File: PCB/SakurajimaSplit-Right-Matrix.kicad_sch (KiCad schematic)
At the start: 42 parts

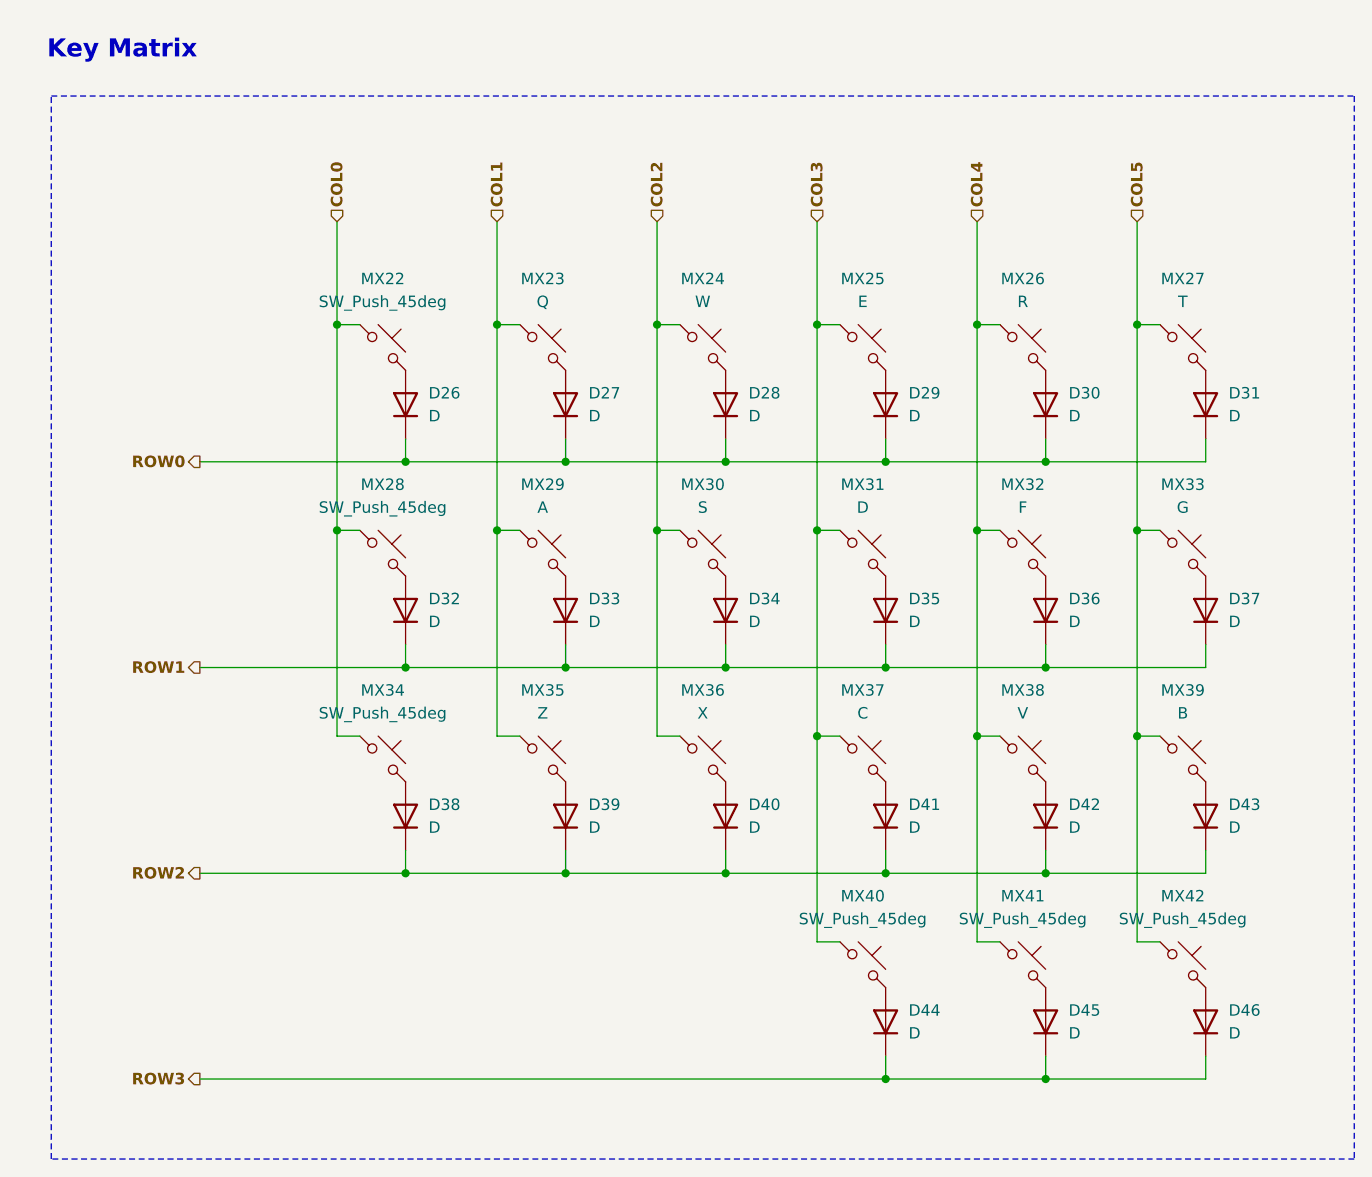
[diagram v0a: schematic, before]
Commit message: feat(sch): design right half of the keyboard
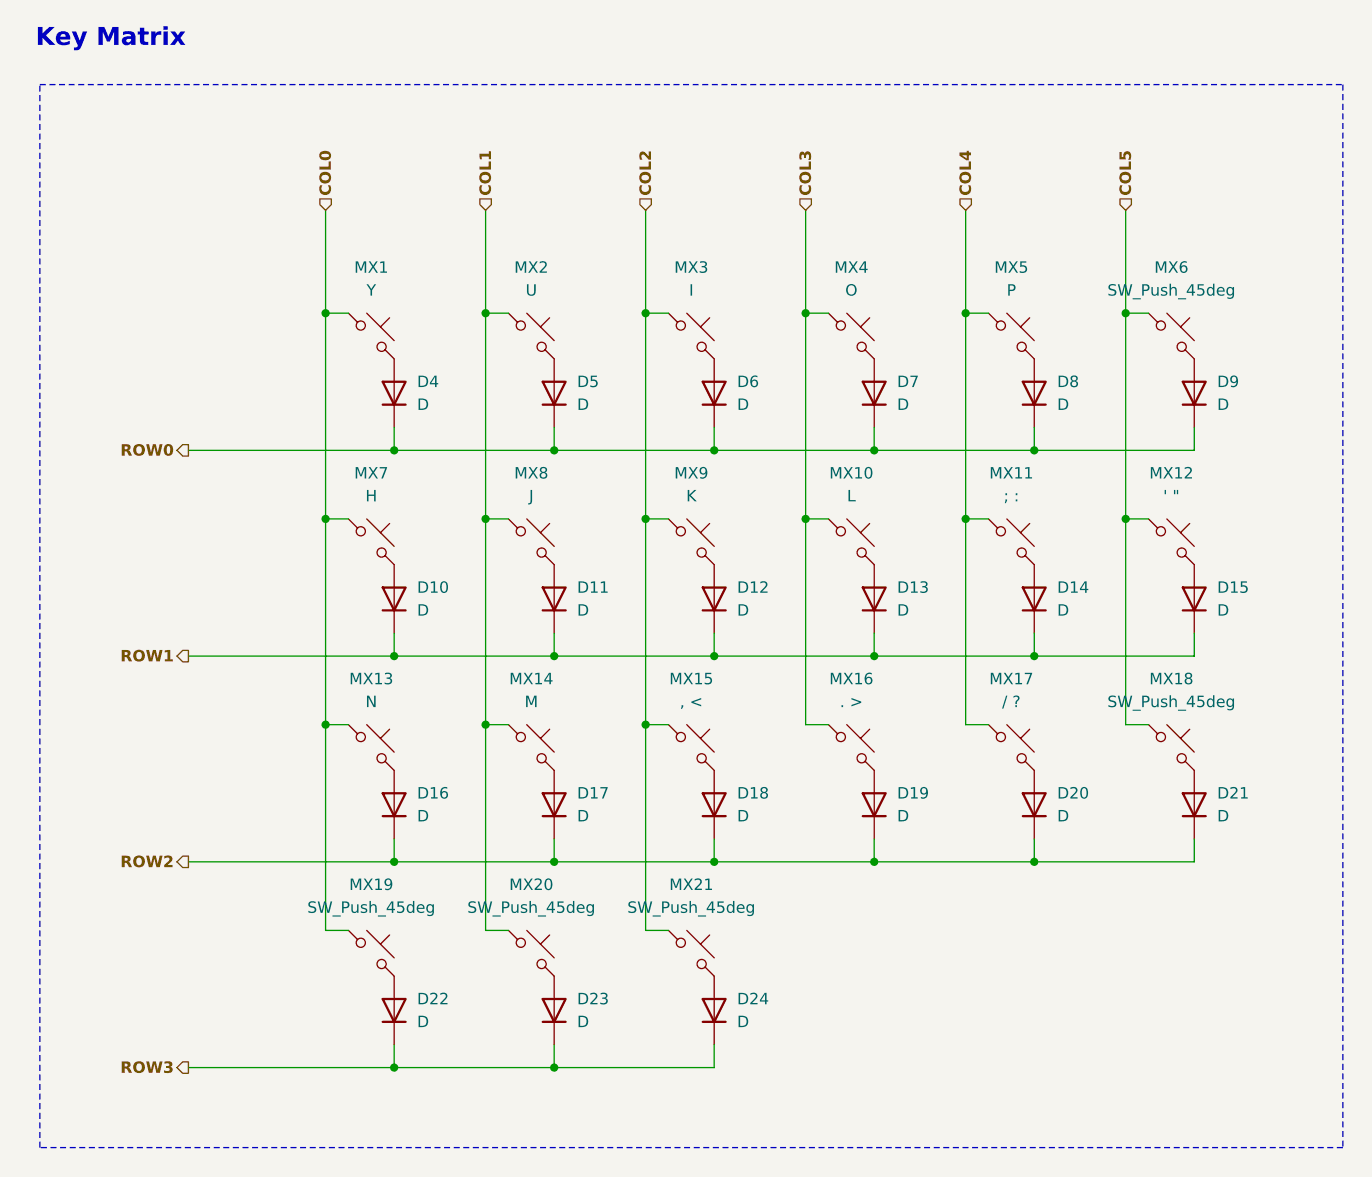
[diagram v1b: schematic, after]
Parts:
- removed D26, D27, D28, D29, D30, D31, D32, D33, D34, D35, D36, D37, D38, D39, D40, D41, D42, D43, D44, D45, D46: D, symbol Device:D
- removed MX22, MX28, MX34, MX40, MX41, MX42: SW_Push_45deg, symbol Switch:SW_Push_45deg
- removed MX23: Q, symbol Switch:SW_Push_45deg
- removed MX24: W, symbol Switch:SW_Push_45deg
- removed MX25: E, symbol Switch:SW_Push_45deg
- removed MX26: R, symbol Switch:SW_Push_45deg
- removed MX27: T, symbol Switch:SW_Push_45deg
- removed MX29: A, symbol Switch:SW_Push_45deg
- removed MX30: S, symbol Switch:SW_Push_45deg
- removed MX31: D, symbol Switch:SW_Push_45deg
- removed MX32: F, symbol Switch:SW_Push_45deg
- removed MX33: G, symbol Switch:SW_Push_45deg
- removed MX35: Z, symbol Switch:SW_Push_45deg
- removed MX36: X, symbol Switch:SW_Push_45deg
- removed MX37: C, symbol Switch:SW_Push_45deg
- removed MX38: V, symbol Switch:SW_Push_45deg
- removed MX39: B, symbol Switch:SW_Push_45deg
- added D10, D11, D12, D13, D14, D15, D16, D17, D18, D19, D20, D21, D22, D23, D24, D4, D5, D6, D7, D8, D9: D, symbol Device:D
- added MX1: Y, symbol Switch:SW_Push_45deg
- added MX10: L, symbol Switch:SW_Push_45deg
- added MX11: ; :, symbol Switch:SW_Push_45deg
- added MX12: ' ", symbol Switch:SW_Push_45deg
- added MX13: N, symbol Switch:SW_Push_45deg
- added MX14: M, symbol Switch:SW_Push_45deg
- added MX15: , <, symbol Switch:SW_Push_45deg
- added MX16: . >, symbol Switch:SW_Push_45deg
- added MX17: / ?, symbol Switch:SW_Push_45deg
- added MX18, MX19, MX20, MX21, MX6: SW_Push_45deg, symbol Switch:SW_Push_45deg
- added MX2: U, symbol Switch:SW_Push_45deg
- added MX3: I, symbol Switch:SW_Push_45deg
- added MX4: O, symbol Switch:SW_Push_45deg
- added MX5: P, symbol Switch:SW_Push_45deg
- added MX7: H, symbol Switch:SW_Push_45deg
- added MX8: J, symbol Switch:SW_Push_45deg
- added MX9: K, symbol Switch:SW_Push_45deg
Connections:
- net COL0: now also MX1.1, MX13.1, MX19.1, MX7.1
- net COL1: now also MX14.1, MX2.1, MX20.1, MX8.1
- net COL2: now also MX15.1, MX21.1, MX3.1, MX9.1
- net COL3: now also MX10.1, MX16.1, MX4.1
- net COL4: now also MX11.1, MX17.1, MX5.1
- net COL5: now also MX12.1, MX18.1, MX6.1
- net ROW0: now also D4.1 (K), D5.1 (K), D6.1 (K), D7.1 (K), D8.1 (K), D9.1 (K)
- net ROW1: now also D10.1 (K), D11.1 (K), D12.1 (K), D13.1 (K), D14.1 (K), D15.1 (K)
- net ROW2: now also D16.1 (K), D17.1 (K), D18.1 (K), D19.1 (K), D20.1 (K), D21.1 (K)
- net ROW3: now also D22.1 (K), D23.1 (K), D24.1 (K)
- new net: D4.2 (A), MX1.2
- new net: D11.2 (A), MX8.2
- new net: D17.2 (A), MX14.2
- new net: D8.2 (A), MX5.2
- new net: D19.2 (A), MX16.2
- new net: D21.2 (A), MX18.2
- new net: D10.2 (A), MX7.2
- new net: D6.2 (A), MX3.2
- new net: D7.2 (A), MX4.2
- new net: D24.2 (A), MX21.2
- new net: D23.2 (A), MX20.2
- new net: D15.2 (A), MX12.2
- new net: D14.2 (A), MX11.2
- new net: D22.2 (A), MX19.2
- new net: D5.2 (A), MX2.2
- new net: D12.2 (A), MX9.2
- new net: D13.2 (A), MX10.2
- new net: D9.2 (A), MX6.2
- new net: D16.2 (A), MX13.2
- new net: D20.2 (A), MX17.2
- new net: D18.2 (A), MX15.2

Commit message: feat(pcb): assign all footprints
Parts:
- D28: renamed from D4; footprint (none) -> Diode_SMD:D_SOD-123
- D29: renamed from D5; footprint (none) -> Diode_SMD:D_SOD-123
- D30: renamed from D6; footprint (none) -> Diode_SMD:D_SOD-123
- D31: renamed from D7; footprint (none) -> Diode_SMD:D_SOD-123
- D32: renamed from D8; footprint (none) -> Diode_SMD:D_SOD-123
- D33: renamed from D9; footprint (none) -> Diode_SMD:D_SOD-123
- D34: renamed from D10; footprint (none) -> Diode_SMD:D_SOD-123
- D35: renamed from D11; footprint (none) -> Diode_SMD:D_SOD-123
- D36: renamed from D12; footprint (none) -> Diode_SMD:D_SOD-123
- D37: renamed from D13; footprint (none) -> Diode_SMD:D_SOD-123
- D38: renamed from D14; footprint (none) -> Diode_SMD:D_SOD-123
- D39: renamed from D15; footprint (none) -> Diode_SMD:D_SOD-123
- D40: renamed from D16; footprint (none) -> Diode_SMD:D_SOD-123
- D41: renamed from D17; footprint (none) -> Diode_SMD:D_SOD-123
- D42: renamed from D18; footprint (none) -> Diode_SMD:D_SOD-123
- D43: renamed from D19; footprint (none) -> Diode_SMD:D_SOD-123
- D44: renamed from D20; footprint (none) -> Diode_SMD:D_SOD-123
- D45: renamed from D21; footprint (none) -> Diode_SMD:D_SOD-123
- D46: renamed from D22; footprint (none) -> Diode_SMD:D_SOD-123
- D47: renamed from D23; footprint (none) -> Diode_SMD:D_SOD-123
- D48: renamed from D24; footprint (none) -> Diode_SMD:D_SOD-123
- MX22: renamed from MX1; footprint (none) -> PCM_marbastlib-mx:SW_MX_1u
- MX23: renamed from MX2; footprint (none) -> PCM_marbastlib-mx:SW_MX_1u
- MX24: renamed from MX3; footprint (none) -> PCM_marbastlib-mx:SW_MX_1u
- MX25: renamed from MX4; footprint (none) -> PCM_marbastlib-mx:SW_MX_1u
- MX26: renamed from MX5; footprint (none) -> PCM_marbastlib-mx:SW_MX_1u
- MX27: renamed from MX6; footprint (none) -> PCM_marbastlib-mx:SW_MX_1u
- MX28: renamed from MX7; footprint (none) -> PCM_marbastlib-mx:SW_MX_1u
- MX29: renamed from MX8; footprint (none) -> PCM_marbastlib-mx:SW_MX_1u
- MX30: renamed from MX9; footprint (none) -> PCM_marbastlib-mx:SW_MX_1u
- MX31: renamed from MX10; footprint (none) -> PCM_marbastlib-mx:SW_MX_1u
- MX32: renamed from MX11; footprint (none) -> PCM_marbastlib-mx:SW_MX_1u
- MX33: renamed from MX12; footprint (none) -> PCM_marbastlib-mx:SW_MX_1u
- MX34: renamed from MX13; footprint (none) -> PCM_marbastlib-mx:SW_MX_1u
- MX35: renamed from MX14; footprint (none) -> PCM_marbastlib-mx:SW_MX_1u
- MX36: renamed from MX15; footprint (none) -> PCM_marbastlib-mx:SW_MX_1u
- MX37: renamed from MX16; footprint (none) -> PCM_marbastlib-mx:SW_MX_1u
- MX38: renamed from MX17; footprint (none) -> PCM_marbastlib-mx:SW_MX_1u
- MX39: renamed from MX18; footprint (none) -> PCM_marbastlib-mx:SW_MX_1u
- MX40: renamed from MX19; footprint (none) -> PCM_marbastlib-mx:SW_MX_1u
- MX41: renamed from MX20; footprint (none) -> PCM_marbastlib-mx:SW_MX_1u
- MX42: renamed from MX21; footprint (none) -> PCM_marbastlib-mx:SW_MX_1u

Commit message: fix(sch): fix matrix diode designators not starting from 1
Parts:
- renumbered D28 to D22, D29 to D23, D30 to D24, D31 to D25, D32 to D26, D33 to D27, D34 to D28, D35 to D29, D36 to D30, D37 to D31, D38 to D32, D39 to D33, D40 to D34, D41 to D35, D42 to D36, D43 to D37, D44 to D38, D45 to D39, D46 to D40, D47 to D41, D48 to D42
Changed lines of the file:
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@@
 		(dnp no)
 		(fields_autoplaced yes)
-		(property "Reference" "D28"
+		(property "Reference" "D22"
 			(at 177.8 111.7599 90)
 			(effects
@@
 			(project "SakurajimaSplit"
 				(path "/2049b6de-7453-46e1-ab60-70116abff9d6/2fb40ee0-3e4b-4e2d-8d4c-b78786a3c10e/177a5d22-8137-4d36-99f5-f50b13e7348e"
-					(reference "D28")
+					(reference "D22")
 					(unit 1)
 				)
@@
 		(dnp no)
 		(fields_autoplaced yes)
-		(property "Reference" "D35"
+		(property "Reference" "D29"
 			(at 195.58 134.6199 90)
 			(effects
@@
 			(project "SakurajimaSplit"
 				(path "/2049b6de-7453-46e1-ab60-70116abff9d6/2fb40ee0-3e4b-4e2d-8d4c-b78786a3c10e/177a5d22-8137-4d36-99f5-f50b13e7348e"
-					(reference "D35")
+					(reference "D29")
 					(unit 1)
 				)
@@
 		(dnp no)
 		(fields_autoplaced yes)
-		(property "Reference" "D41"
+		(property "Reference" "D35"
 			(at 195.58 157.4799 90)
 			(effects
@@
 			(project "SakurajimaSplit"
 				(path "/2049b6de-7453-46e1-ab60-70116abff9d6/2fb40ee0-3e4b-4e2d-8d4c-b78786a3c10e/177a5d22-8137-4d36-99f5-f50b13e7348e"
-					(reference "D41")
+					(reference "D35")
 					(unit 1)
 				)
@@
 		(dnp no)
 		(fields_autoplaced yes)
-		(property "Reference" "D32"
+		(property "Reference" "D26"
 			(at 248.92 111.7599 90)
 			(effects
@@
 			(project "SakurajimaSplit"
 				(path "/2049b6de-7453-46e1-ab60-70116abff9d6/2fb40ee0-3e4b-4e2d-8d4c-b78786a3c10e/177a5d22-8137-4d36-99f5-f50b13e7348e"
-					(reference "D32")
+					(reference "D26")
 					(unit 1)
 				)
@@
 		(dnp no)
 		(fields_autoplaced yes)
-		(property "Reference" "D45"
+		(property "Reference" "D39"
 			(at 266.7 157.4799 90)
 			(effects
@@
 			(project "SakurajimaSplit"
 				(path "/2049b6de-7453-46e1-ab60-70116abff9d6/2fb40ee0-3e4b-4e2d-8d4c-b78786a3c10e/177a5d22-8137-4d36-99f5-f50b13e7348e"
-					(reference "D45")
+					(reference "D39")
 					(unit 1)
 				)
@@
 		(dnp no)
 		(fields_autoplaced yes)
-		(property "Reference" "D30"
+		(property "Reference" "D24"
 			(at 213.36 111.7599 90)
 			(effects
@@
 			(project "SakurajimaSplit"
 				(path "/2049b6de-7453-46e1-ab60-70116abff9d6/2fb40ee0-3e4b-4e2d-8d4c-b78786a3c10e/177a5d22-8137-4d36-99f5-f50b13e7348e"
-					(reference "D30")
+					(reference "D24")
 					(unit 1)
 				)
@@
 		(dnp no)
 		(fields_autoplaced yes)
-		(property "Reference" "D39"
+		(property "Reference" "D33"
 			(at 266.7 134.6199 90)
 			(effects
@@
 			(project "SakurajimaSplit"
 				(path "/2049b6de-7453-46e1-ab60-70116abff9d6/2fb40ee0-3e4b-4e2d-8d4c-b78786a3c10e/177a5d22-8137-4d36-99f5-f50b13e7348e"
-					(reference "D39")
+					(reference "D33")
 					(unit 1)
 				)
@@
 		(dnp no)
 		(fields_autoplaced yes)
-		(property "Reference" "D46"
+		(property "Reference" "D40"
 			(at 177.8 180.3399 90)
 			(effects
@@
 			(project "SakurajimaSplit"
 				(path "/2049b6de-7453-46e1-ab60-70116abff9d6/2fb40ee0-3e4b-4e2d-8d4c-b78786a3c10e/177a5d22-8137-4d36-99f5-f50b13e7348e"
-					(reference "D46")
+					(reference "D40")
 					(unit 1)
 				)
@@
 		(dnp no)
 		(fields_autoplaced yes)
-		(property "Reference" "D29"
+		(property "Reference" "D23"
 			(at 195.58 111.7599 90)
 			(effects
@@
 			(project "SakurajimaSplit"
 				(path "/2049b6de-7453-46e1-ab60-70116abff9d6/2fb40ee0-3e4b-4e2d-8d4c-b78786a3c10e/177a5d22-8137-4d36-99f5-f50b13e7348e"
-					(reference "D29")
+					(reference "D23")
 					(unit 1)
 				)
@@
 		(dnp no)
 		(fields_autoplaced yes)
-		(property "Reference" "D38"
+		(property "Reference" "D32"
 			(at 248.92 134.6199 90)
 			(effects
@@
 			(project "SakurajimaSplit"
 				(path "/2049b6de-7453-46e1-ab60-70116abff9d6/2fb40ee0-3e4b-4e2d-8d4c-b78786a3c10e/177a5d22-8137-4d36-99f5-f50b13e7348e"
-					(reference "D38")
+					(reference "D32")
 					(unit 1)
 				)
@@
 		(dnp no)
 		(fields_autoplaced yes)
-		(property "Reference" "D48"
+		(property "Reference" "D42"
 			(at 213.36 180.3399 90)
 			(effects
@@
 			(project "SakurajimaSplit"
 				(path "/2049b6de-7453-46e1-ab60-70116abff9d6/2fb40ee0-3e4b-4e2d-8d4c-b78786a3c10e/177a5d22-8137-4d36-99f5-f50b13e7348e"
-					(reference "D48")
+					(reference "D42")
 					(unit 1)
 				)
@@
 		(dnp no)
 		(fields_autoplaced yes)
-		(property "Reference" "D34"
+		(property "Reference" "D28"
 			(at 177.8 134.6199 90)
 			(effects
@@
 			(project "SakurajimaSplit"
 				(path "/2049b6de-7453-46e1-ab60-70116abff9d6/2fb40ee0-3e4b-4e2d-8d4c-b78786a3c10e/177a5d22-8137-4d36-99f5-f50b13e7348e"
-					(reference "D34")
+					(reference "D28")
 					(unit 1)
 				)
@@
 		(dnp no)
 		(fields_autoplaced yes)
-		(property "Reference" "D43"
+		(property "Reference" "D37"
 			(at 231.14 157.4799 90)
 			(effects
@@
 			(project "SakurajimaSplit"
 				(path "/2049b6de-7453-46e1-ab60-70116abff9d6/2fb40ee0-3e4b-4e2d-8d4c-b78786a3c10e/177a5d22-8137-4d36-99f5-f50b13e7348e"
-					(reference "D43")
+					(reference "D37")
 					(unit 1)
 				)
@@
 		(dnp no)
 		(fields_autoplaced yes)
-		(property "Reference" "D37"
+		(property "Reference" "D31"
 			(at 231.14 134.6199 90)
 			(effects
@@
 			(project "SakurajimaSplit"
 				(path "/2049b6de-7453-46e1-ab60-70116abff9d6/2fb40ee0-3e4b-4e2d-8d4c-b78786a3c10e/177a5d22-8137-4d36-99f5-f50b13e7348e"
-					(reference "D37")
+					(reference "D31")
 					(unit 1)
 				)
@@
 		(dnp no)
 		(fields_autoplaced yes)
-		(property "Reference" "D33"
+		(property "Reference" "D27"
 			(at 266.7 111.7599 90)
 			(effects
@@
 			(project "SakurajimaSplit"
 				(path "/2049b6de-7453-46e1-ab60-70116abff9d6/2fb40ee0-3e4b-4e2d-8d4c-b78786a3c10e/177a5d22-8137-4d36-99f5-f50b13e7348e"
-					(reference "D33")
+					(reference "D27")
 					(unit 1)
 				)
@@
 		(dnp no)
 		(fields_autoplaced yes)
-		(property "Reference" "D31"
+		(property "Reference" "D25"
 			(at 231.14 111.7599 90)
 			(effects
@@
 			(project "SakurajimaSplit"
 				(path "/2049b6de-7453-46e1-ab60-70116abff9d6/2fb40ee0-3e4b-4e2d-8d4c-b78786a3c10e/177a5d22-8137-4d36-99f5-f50b13e7348e"
-					(reference "D31")
+					(reference "D25")
 					(unit 1)
 				)
@@
 		(dnp no)
 		(fields_autoplaced yes)
-		(property "Reference" "D40"
+		(property "Reference" "D34"
 			(at 177.8 157.4799 90)
 			(effects
@@
 			(project "SakurajimaSplit"
 				(path "/2049b6de-7453-46e1-ab60-70116abff9d6/2fb40ee0-3e4b-4e2d-8d4c-b78786a3c10e/177a5d22-8137-4d36-99f5-f50b13e7348e"
-					(reference "D40")
+					(reference "D34")
 					(unit 1)
 				)
@@
 		(dnp no)
 		(fields_autoplaced yes)
-		(property "Reference" "D36"
+		(property "Reference" "D30"
 			(at 213.36 134.6199 90)
 			(effects
@@
 			(project "SakurajimaSplit"
 				(path "/2049b6de-7453-46e1-ab60-70116abff9d6/2fb40ee0-3e4b-4e2d-8d4c-b78786a3c10e/177a5d22-8137-4d36-99f5-f50b13e7348e"
-					(reference "D36")
+					(reference "D30")
 					(unit 1)
 				)
@@
 		(dnp no)
 		(fields_autoplaced yes)
-		(property "Reference" "D42"
+		(property "Reference" "D36"
 			(at 213.36 157.4799 90)
 			(effects
@@
 			(project "SakurajimaSplit"
 				(path "/2049b6de-7453-46e1-ab60-70116abff9d6/2fb40ee0-3e4b-4e2d-8d4c-b78786a3c10e/177a5d22-8137-4d36-99f5-f50b13e7348e"
-					(reference "D42")
+					(reference "D36")
 					(unit 1)
 				)
@@
 		(dnp no)
 		(fields_autoplaced yes)
-		(property "Reference" "D47"
+		(property "Reference" "D41"
 			(at 195.58 180.3399 90)
 			(effects
@@
 			(project "SakurajimaSplit"
 				(path "/2049b6de-7453-46e1-ab60-70116abff9d6/2fb40ee0-3e4b-4e2d-8d4c-b78786a3c10e/177a5d22-8137-4d36-99f5-f50b13e7348e"
-					(reference "D47")
+					(reference "D41")
 					(unit 1)
 				)
@@
 		(dnp no)
 		(fields_autoplaced yes)
-		(property "Reference" "D44"
+		(property "Reference" "D38"
 			(at 248.92 157.4799 90)
 			(effects
@@
 			(project "SakurajimaSplit"
 				(path "/2049b6de-7453-46e1-ab60-70116abff9d6/2fb40ee0-3e4b-4e2d-8d4c-b78786a3c10e/177a5d22-8137-4d36-99f5-f50b13e7348e"
-					(reference "D44")
+					(reference "D38")
 					(unit 1)
 				)

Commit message: fix(sch): fix wrong footprint for MX21 & MX40
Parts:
- MX40: footprint PCM_marbastlib-mx:SW_MX_1u -> PCM_marbastlib-mx:SW_MX_1.5u
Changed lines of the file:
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@@
 			)
 		)
-		(property "Footprint" "PCM_marbastlib-mx:SW_MX_1u"
+		(property "Footprint" "PCM_marbastlib-mx:SW_MX_1.5u"
 			(at 172.72 175.26 0)
 			(effects
